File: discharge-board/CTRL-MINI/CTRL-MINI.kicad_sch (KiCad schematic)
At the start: 16 parts, among them J1 MD1-L, J10 MD2-R, J11 Conn_01x04_Pin, J12 Conn_01x04_Pin, J2 Screw_Terminal_01x02, J3 MD0-L, J4 MD0-R, J5 RPP-L, J6 RPP-R, J7 MD1-R, J8 Conn_01x04_Pin, J9 MD2-L, U1 BD50FC0FP

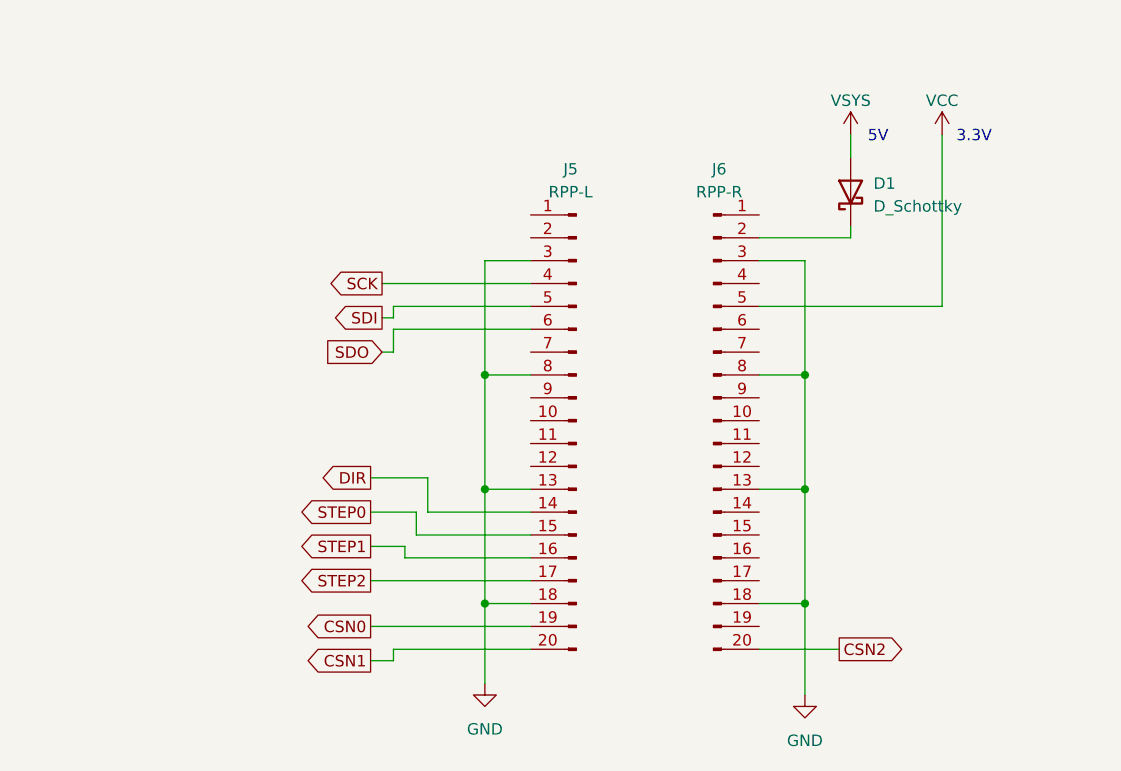
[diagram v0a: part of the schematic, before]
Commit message: Optimize RPP pin assignment and reserve UART0 & SPI1
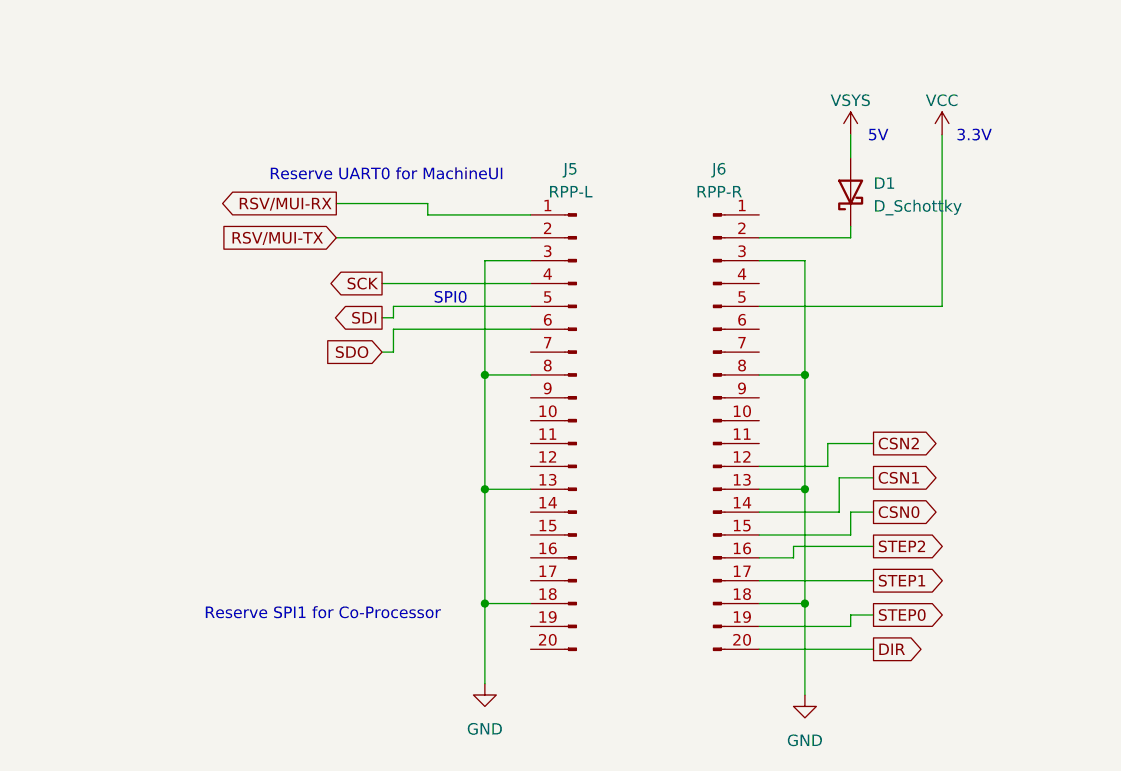
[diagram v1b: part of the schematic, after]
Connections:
- net CSN0: now also J6.15 (Pin_15); no longer J5.19 (Pin_19)
- net CSN1: now also J6.14 (Pin_14); no longer J5.20 (Pin_20)
- net CSN2: now also J6.12 (Pin_12); no longer J6.20 (Pin_20)
- net DIR: now also J6.20 (Pin_20); no longer J5.14 (Pin_14)
- net STEP0: now also J6.19 (Pin_19); no longer J5.15 (Pin_15)
- net STEP1: now also J6.17 (Pin_17); no longer J5.16 (Pin_16)
- net STEP2: now also J6.16 (Pin_16); no longer J5.17 (Pin_17)
- net RSV/MUI-RX: now reaches J5.1 (Pin_1)
- net RSV/MUI-TX: now reaches J5.2 (Pin_2)
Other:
- note added: "Reserve SPI1 for Co-Processor"
- note added: "Reserve UART0 for MachineUI"
- note added: "SPI0"

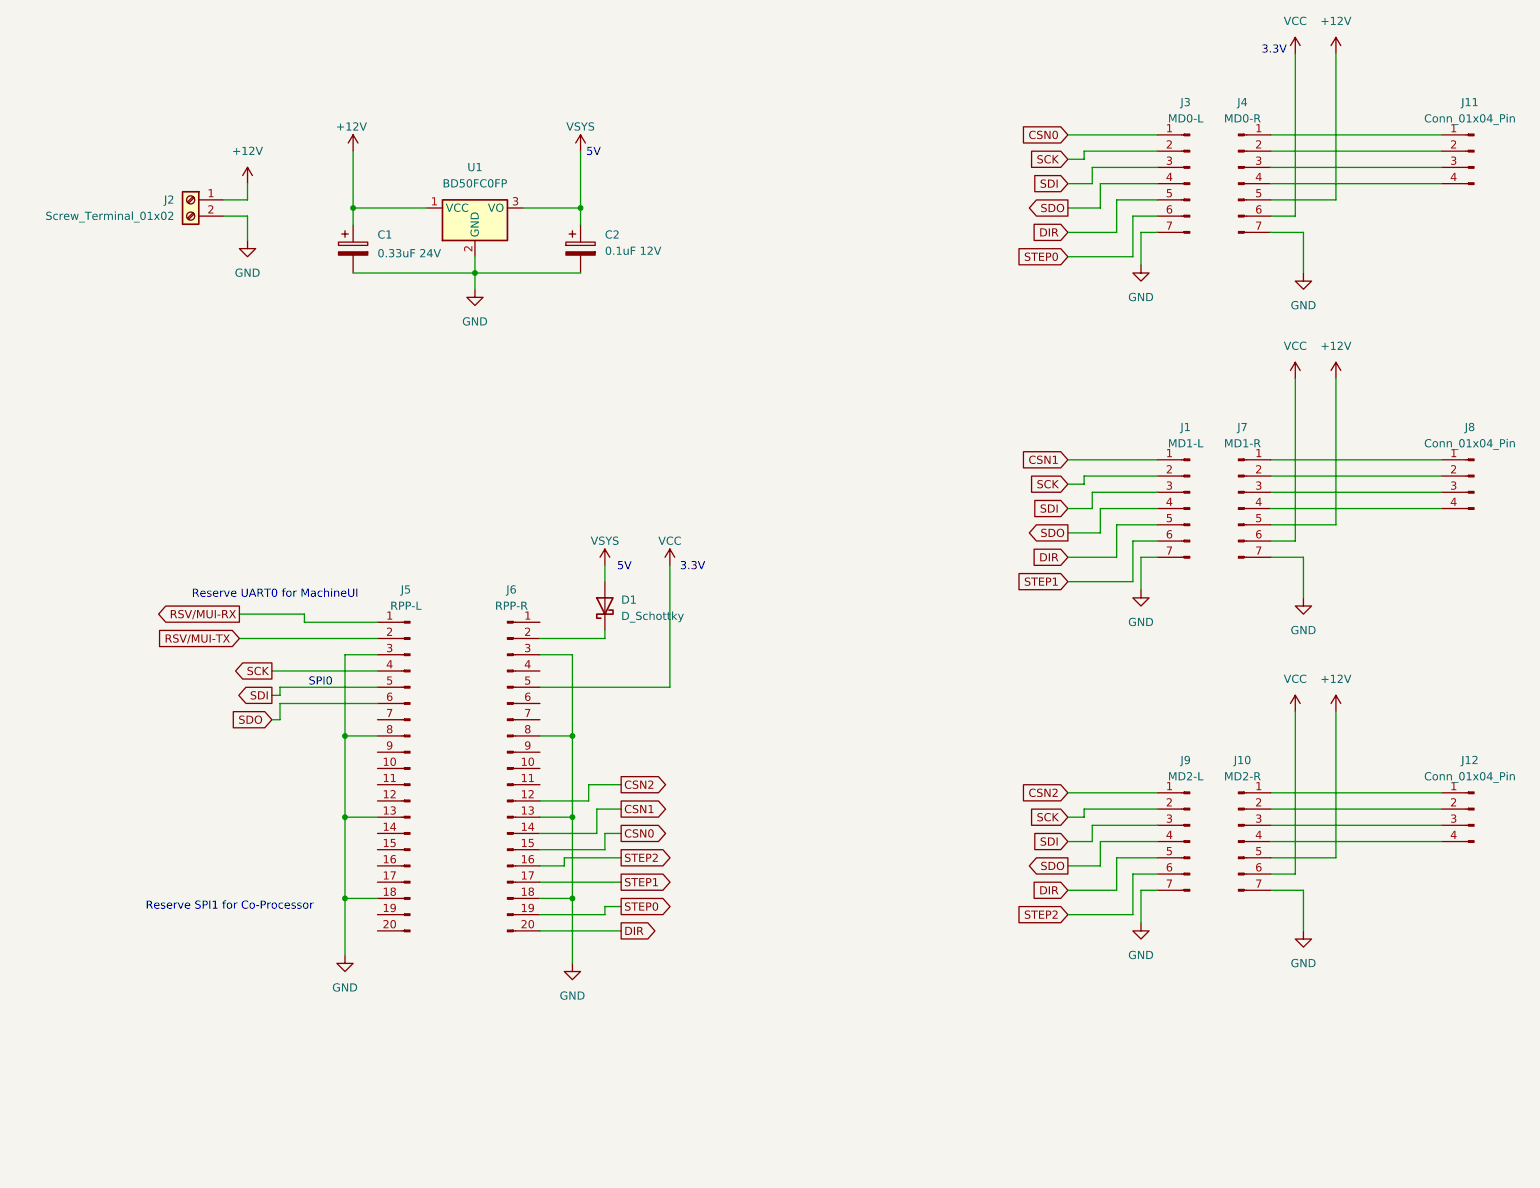
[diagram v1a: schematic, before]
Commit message: CTRL-MINI PCB r0 passed DRC as 2-layer
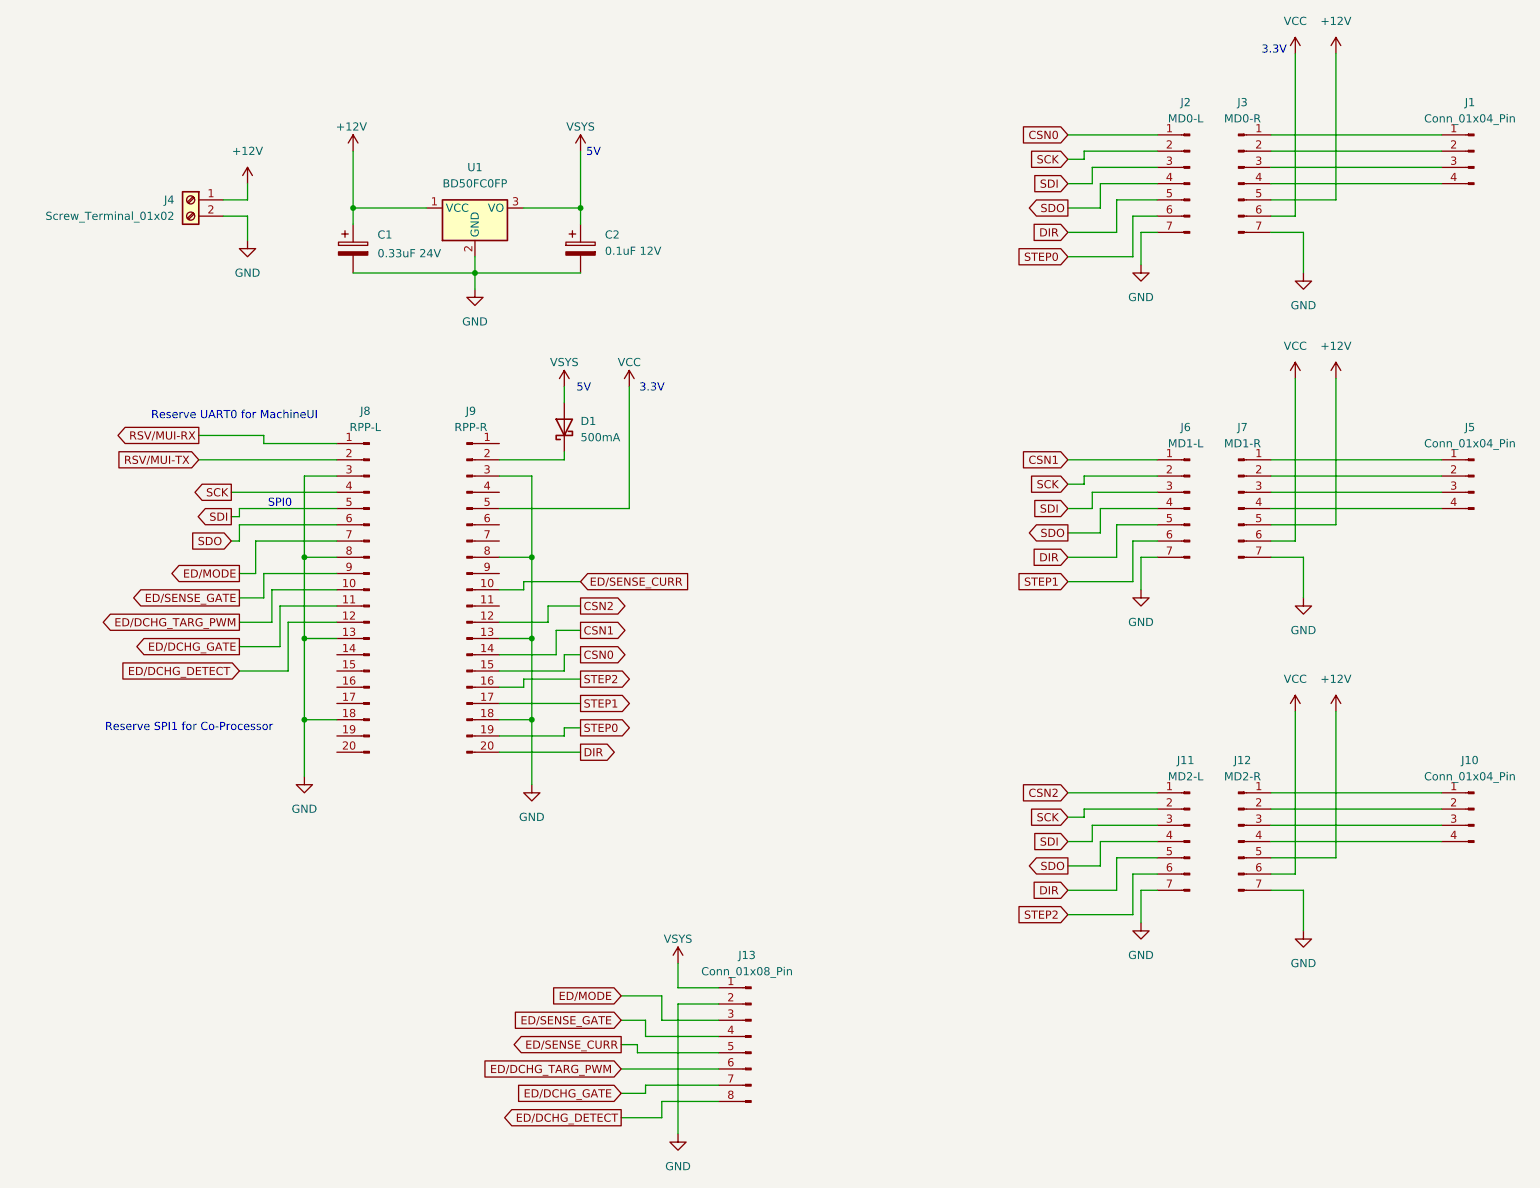
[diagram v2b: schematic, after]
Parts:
- added J13: Conn_01x08_Pin, SparkAll:CON_526100872_MOL, symbol Connector:Conn_01x08_Pin
- C1, C2: footprint (none) -> Resistor_SMD:R_0603_1608Metric
- D1: value D_Schottky -> 500mA; footprint (none) -> Diode_SMD:D_0805_2012Metric
- J1: renamed from J11; footprint (none) -> Connector_JST:JST_XH_B4B-XH-A_1x04_P2.50mm_Vertical
- J10: renamed from J12; footprint (none) -> Connector_JST:JST_XH_B4B-XH-A_1x04_P2.50mm_Vertical
- J11: renamed from J9; footprint (none) -> Connector_PinSocket_2.54mm:PinSocket_1x07_P2.54mm_Vertical
- J12: renamed from J10; footprint (none) -> Connector_PinSocket_2.54mm:PinSocket_1x07_P2.54mm_Vertical
- J2: renamed from J3; footprint (none) -> Connector_PinSocket_2.54mm:PinSocket_1x07_P2.54mm_Vertical
- J3: renamed from J4; footprint (none) -> Connector_PinSocket_2.54mm:PinSocket_1x07_P2.54mm_Vertical
- J4: renamed from J2; footprint (none) -> SparkAll:691137710002
- J5: renamed from J8; footprint (none) -> Connector_JST:JST_XH_B4B-XH-A_1x04_P2.50mm_Vertical
- J6: renamed from J1; footprint (none) -> Connector_PinSocket_2.54mm:PinSocket_1x07_P2.54mm_Vertical
- J7: footprint (none) -> Connector_PinSocket_2.54mm:PinSocket_1x07_P2.54mm_Vertical
- J9: renamed from J6; footprint (none) -> Connector_PinSocket_2.54mm:PinSocket_1x20_P2.54mm_Vertical
- renumbered J5 to J8
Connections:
- net GND: now also J13.2 (Pin_2)
- net VSYS: now also J13.1 (Pin_1)
- net ED/SENSE_CURR: now reaches J9.10 (Pin_10)
- net ED/SENSE_CURR: now also J13.5 (Pin_5)
- net ED/DCHG_TARG_PWM: now reaches J8.10 (Pin_10)
- net ED/DCHG_TARG_PWM: now also J13.6 (Pin_6)
- net ED/DCHG_GATE: now reaches J8.11 (Pin_11)
- net ED/DCHG_GATE: now also J13.7 (Pin_7)
- net ED/DCHG_DETECT: now reaches J8.12 (Pin_12)
- net ED/DCHG_DETECT: now also J13.8 (Pin_8)
- net ED/MODE: now reaches J8.7 (Pin_7)
- net ED/MODE: now also J13.3 (Pin_3)
- net ED/SENSE_GATE: now reaches J8.9 (Pin_9)
- net ED/SENSE_GATE: now also J13.4 (Pin_4)
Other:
- moved on the sheet: D1, J8, J9

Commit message: Improve manufacturability of MB, use SOD-523
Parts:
- D1: footprint Diode_SMD:D_0805_2012Metric -> Diode_SMD:D_SOD-523
- J1, J10, J5: LCSC (none) -> C144395
- J11, J12, J2, J3, J6, J7: LCSC (none) -> C5371993
- J8, J9: LCSC (none) -> C5224030
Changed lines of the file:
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@@
 			)
 		)
-		(property "Footprint" "Diode_SMD:D_0805_2012Metric"
+		(property "Footprint" "Diode_SMD:D_SOD-523"
 			(at 105.41 78.74 0)
 			(effects
@@
 		)
 		(property "Description" "Schottky diode"
+			(at 105.41 78.74 0)
+			(effects
+				(font
+					(size 1.27 1.27)
+				)
+				(hide yes)
+			)
+		)
+		(property "LCSC" ""
 			(at 105.41 78.74 0)
 			(effects
@@
 			)
 		)
+		(property "LCSC" "C5371993"
+			(at 203.2 91.44 0)
+			(effects
+				(font
+					(size 1.27 1.27)
+				)
+				(hide yes)
+			)
+		)
 		(pin "2"
 		)
@@
 			)
 		)
+		(property "LCSC" "C5371993"
+			(at 203.2 40.64 0)
+			(effects
+				(font
+					(size 1.27 1.27)
+				)
+				(hide yes)
+			)
+		)
 		(pin "2"
 		)
@@
 			)
 		)
+		(property "LCSC" "C5371993"
+			(at 210.82 143.51 0)
+			(effects
+				(font
+					(size 1.27 1.27)
+				)
+				(hide yes)
+			)
+		)
 		(pin "2"
 		)
@@
 			)
 		)
+		(property "LCSC" ""
+			(at 134.62 173.99 0)
+			(effects
+				(font
+					(size 1.27 1.27)
+				)
+				(hide yes)
+			)
+		)
 		(pin "2"
 		)
@@
 			)
 		)
+		(property "LCSC" ""
+			(at 107.95 50.8 0)
+			(effects
+				(font
+					(size 1.27 1.27)
+				)
+				(hide yes)
+			)
+		)
 		(pin "2"
 		)
@@
 			)
 		)
+		(property "LCSC" ""
+			(at 46.99 43.18 0)
+			(effects
+				(font
+					(size 1.27 1.27)
+				)
+				(hide yes)
+			)
+		)
 		(pin "2"
 		)
@@
 			)
 		)
+		(property "LCSC" "C5371993"
+			(at 210.82 91.44 0)
+			(effects
+				(font
+					(size 1.27 1.27)
+				)
+				(hide yes)
+			)
+		)
 		(pin "2"
 		)
@@
 			)
 		)
+		(property "LCSC" "C144395"
+			(at 247.65 138.43 0)
+			(effects
+				(font
+					(size 1.27 1.27)
+				)
+				(hide yes)
+			)
+		)
 		(pin "1"
 		)
@@
 			)
 		)
+		(property "LCSC" ""
+			(at 91.44 44.45 0)
+			(effects
+				(font
+					(size 1.27 1.27)
+				)
+				(hide yes)
+			)
+		)
 		(pin "1"
 		)
@@
 			)
 		)
+		(property "LCSC" "C144395"
+			(at 247.65 35.56 0)
+			(effects
+				(font
+					(size 1.27 1.27)
+				)
+				(hide yes)
+			)
+		)
 		(pin "1"
 		)
@@
 			)
 		)
+		(property "LCSC" "C5371993"
+			(at 203.2 143.51 0)
+			(effects
+				(font
+					(size 1.27 1.27)
+				)
+				(hide yes)
+			)
+		)
 		(pin "2"
 		)
@@
 			)
 		)
+		(property "LCSC" "C5224030"
+			(at 90.17 104.14 0)
+			(effects
+				(font
+					(size 1.27 1.27)
+				)
+				(hide yes)
+			)
+		)
 		(pin "9"
 		)
@@
 			)
 		)
+		(property "LCSC" "C144395"
+			(at 247.65 86.36 0)
+			(effects
+				(font
+					(size 1.27 1.27)
+				)
+				(hide yes)
+			)
+		)
 		(pin "1"
 		)
@@
 			)
 		)
+		(property "LCSC" ""
+			(at 72.39 50.8 0)
+			(effects
+				(font
+					(size 1.27 1.27)
+				)
+				(hide yes)
+			)
+		)
 		(pin "2"
 		)
@@
 			)
 		)
+		(property "LCSC" "C5224030"
+			(at 74.93 104.14 0)
+			(effects
+				(font
+					(size 1.27 1.27)
+				)
+				(hide yes)
+			)
+		)
 		(pin "9"
 		)
@@
 			(at 210.82 40.64 0)
 			(effects
+				(font
+					(size 1.27 1.27)
+				)
+				(hide yes)
+			)
+		)
+		(property "LCSC" "C5371993"
+			(at 210.82 40.64 0)
+			(effects
